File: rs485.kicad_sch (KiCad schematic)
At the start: 48 parts, among them J2101 RS485 Socket, Q2001 2N7002, U2102 ISO7741DBQ, U2104 SP3485EN-L/TR, U2105 SP3485EN-L/TR

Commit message: Fix schematic ERC errors
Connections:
- net GND2 renamed GND_RS485

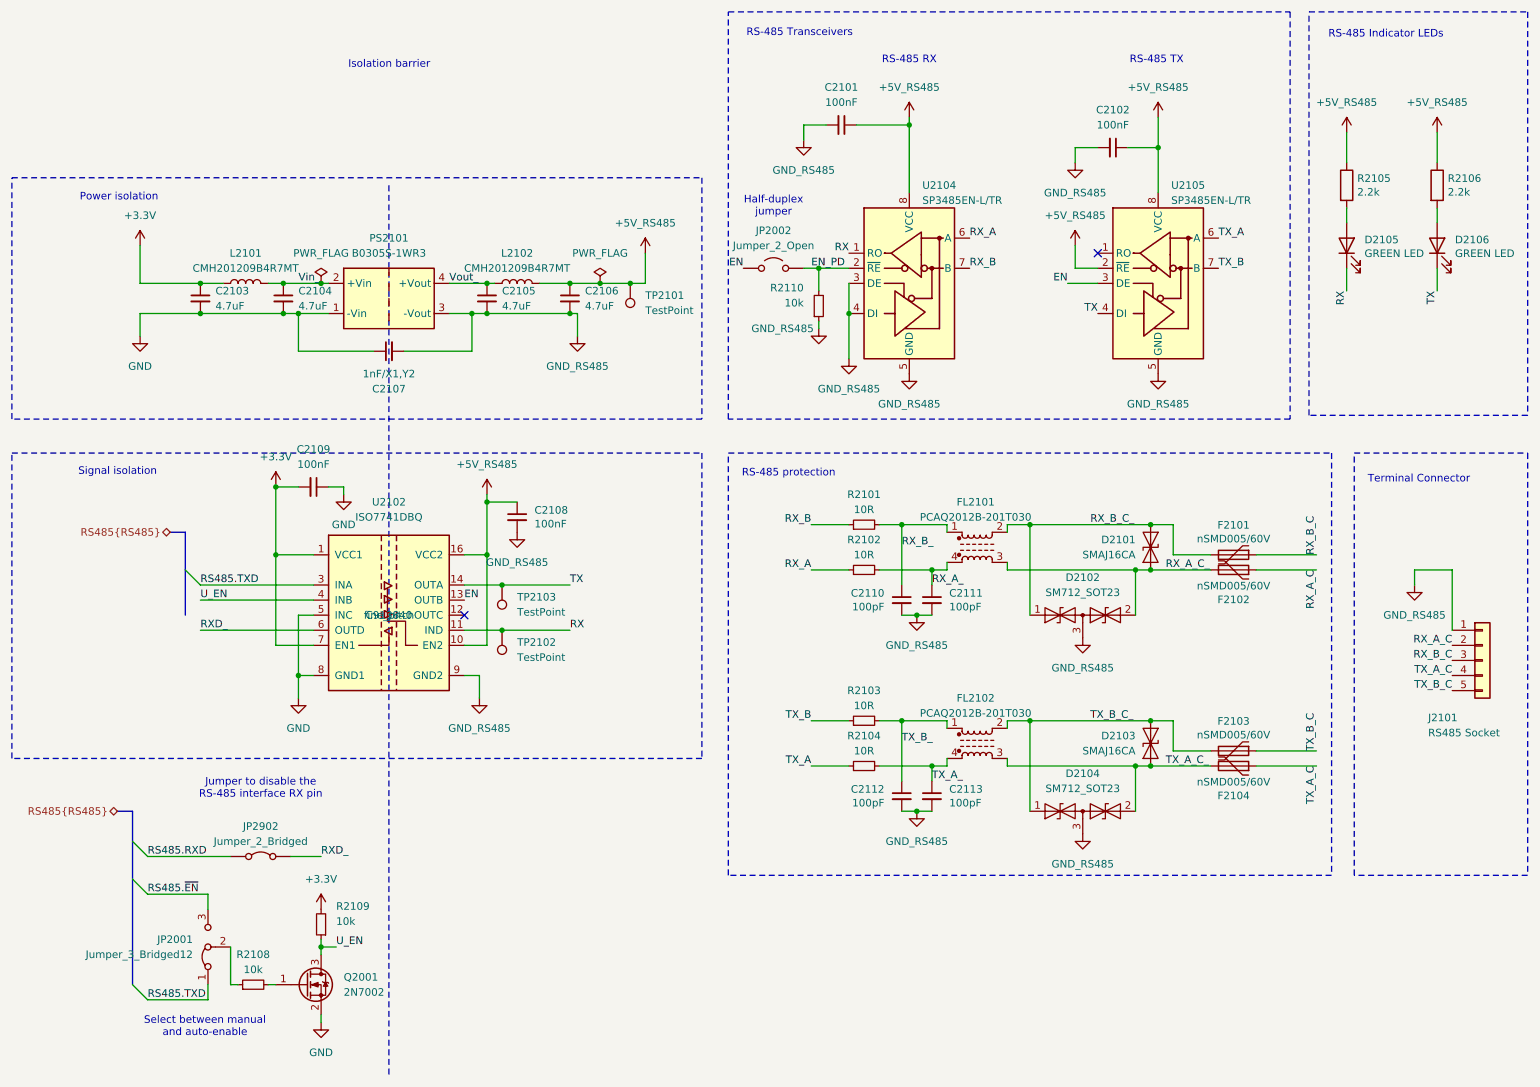
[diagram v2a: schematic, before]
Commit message: Reannotate components
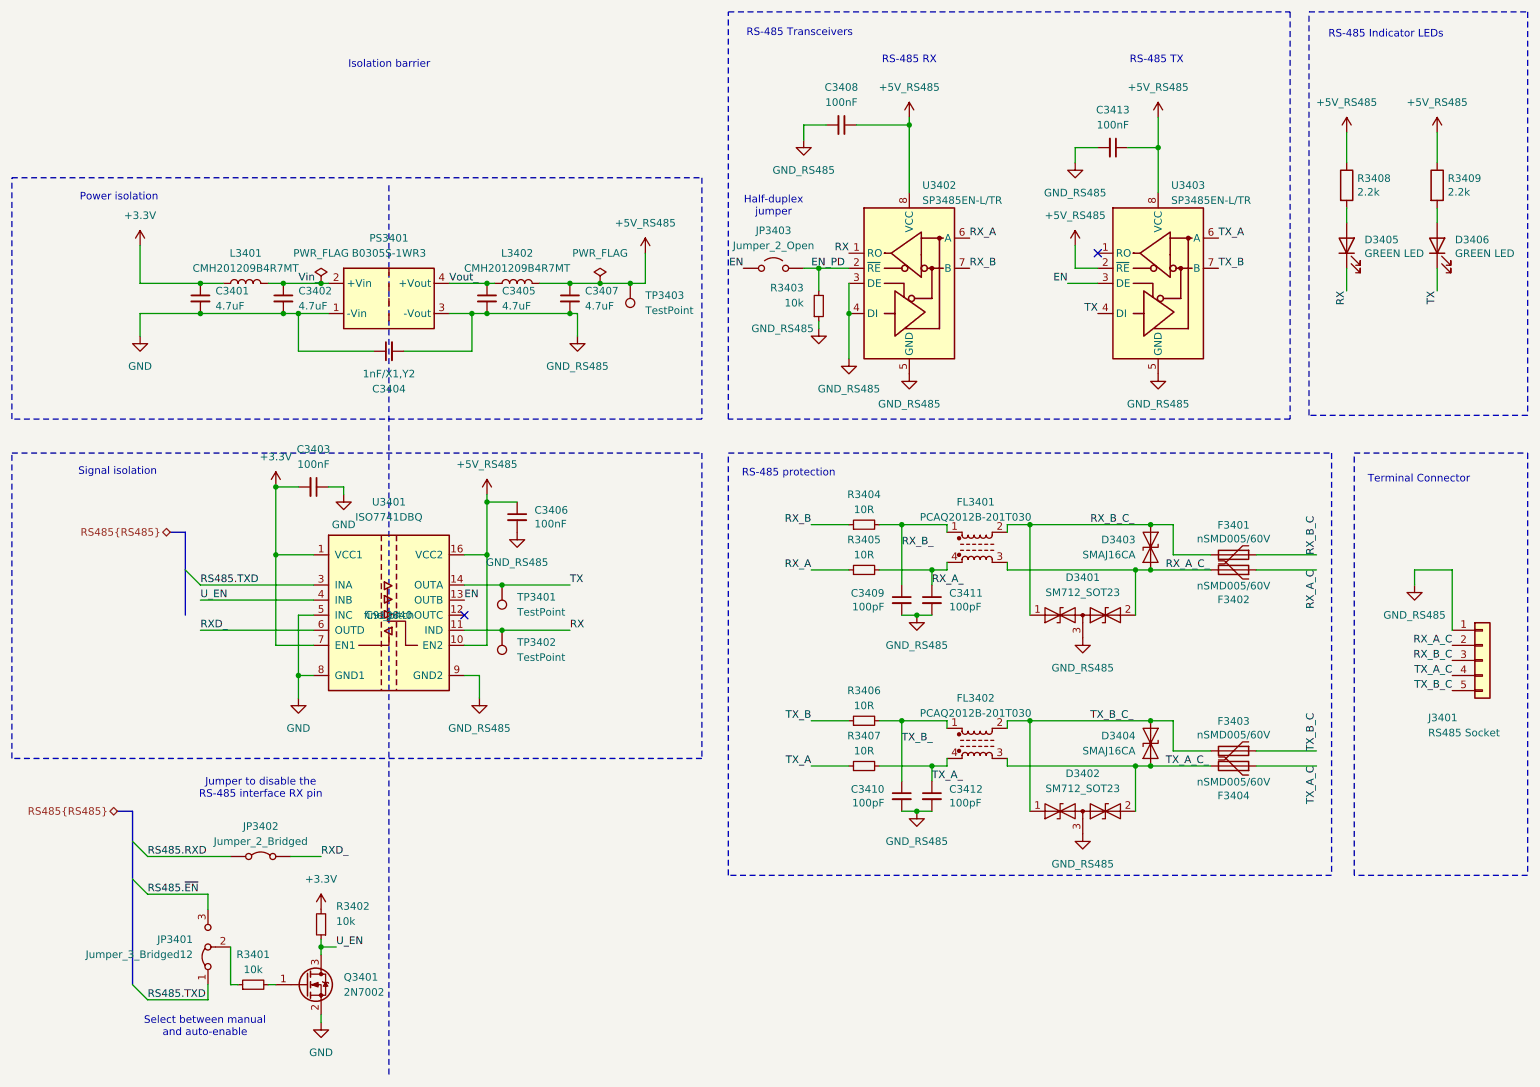
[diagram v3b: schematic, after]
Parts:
- renumbered C2103 to C3401, C2104 to C3402, C2109 to C3403, C2107 to C3404, C2105 to C3405, C2108 to C3406, C2106 to C3407, C2101 to C3408, C2110 to C3409, C2112 to C3410, C2111 to C3411, C2113 to C3412, C2102 to C3413, D2102 to D3401, D2104 to D3402, D2101 to D3403, D2103 to D3404, D2105 to D3405, D2106 to D3406, F2101 to F3401, F2102 to F3402, F2103 to F3403, F2104 to F3404, FL2101 to FL3401, FL2102 to FL3402, J2101 to J3401, JP2001 to JP3401, JP2902 to JP3402, JP2002 to JP3403, L2101 to L3401, L2102 to L3402, PS2101 to PS3401, Q2001 to Q3401, R2108 to R3401, R2109 to R3402, R2110 to R3403, R2101 to R3404, R2102 to R3405, R2103 to R3406, R2104 to R3407, R2105 to R3408, R2106 to R3409, TP2103 to TP3401, TP2102 to TP3402, TP2101 to TP3403, U2102 to U3401, U2104 to U3402, U2105 to U3403

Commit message: Most DRC errors fixed
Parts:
- JP3401: LCSC (none) -> C2937625
- JP3403: LCSC (none) -> C492401
- Q3401: LCSC (none) -> 2N7002
- R3401, R3402, R3403: LCSC (none) -> C25744
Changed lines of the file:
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@@
 		(polyline
 			(pts
-				(xy 54.61 110.49) (xy 54.61 121.92) (xy 52.07 121.92) (xy 52.07 110.49)
+				(xy 109.22 111.76) (xy 109.22 123.19) (xy 106.68 123.19) (xy 106.68 111.76)
 			)
 			(stroke
@@
 		(polyline
 			(pts
-				(xy 109.22 111.76) (xy 109.22 123.19) (xy 106.68 123.19) (xy 106.68 111.76)
+				(xy 54.61 110.49) (xy 54.61 121.92) (xy 52.07 121.92) (xy 52.07 110.49)
 			)
 			(stroke
@@
 			)
 		)
-		(property "LCSC" ""
+		(property "LCSC" "C25744"
 			(at 57.15 180.34 0)
 			(effects
@@
 			)
 		)
+		(property "LCSC" "C2937625"
+			(at 49.53 173.99 0)
+			(effects
+				(font
+					(size 1.27 1.27)
+				)
+			)
+		)
 		(pin "3"
 		)
@@
 			)
 		)
-		(property "LCSC" ""
+		(property "LCSC" "C25744"
 			(at 152.4 66.04 0)
 			(effects
@@
 			)
 		)
-		(property "LCSC" ""
+		(property "LCSC" "C25744"
 			(at 68.58 170.18 0)
 			(effects
@@
 			)
 		)
+		(property "LCSC" "2N7002"
+			(at 66.04 180.34 0)
+			(effects
+				(font
+					(size 1.27 1.27)
+				)
+			)
+		)
 		(pin "3"
 		)
@@
 			)
 		)
+		(property "LCSC" "C492401"
+			(at 144.78 59.69 0)
+			(effects
+				(font
+					(size 1.27 1.27)
+				)
+			)
+		)
 		(pin "2"
 		)
@@
 					(size 1.27 1.27)
 				)
+				(hide yes)
 			)
 		)
@@
 					(size 1.27 1.27)
 				)
+				(hide yes)
 			)
 		)

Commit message: Silkscreen mostly done
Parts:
- C3403, C3406, C3408, C3413: value 100nF -> 1uF; LCSC C1525 -> C52923
- D3402: Component Class (none) -> fine_pitch
- Q3401: LCSC 2N7002 -> C8545
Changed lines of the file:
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@@
 			)
 		)
-		(property "Value" "100nF"
+		(property "Value" "1uF"
 			(at 156.2036 31.75 90)
 			(effects
@@
 			)
 		)
-		(property "LCSC" "C1525"
+		(property "LCSC" "C52923"
 			(at 156.21 35.56 0)
 			(effects
@@
 			)
 		)
+		(property "Component Class" "fine_pitch"
+			(at 196.85 151.13 0)
+			(effects
+				(font
+					(size 1.27 1.27)
+				)
+			)
+		)
 		(pin "3"
 		)
@@
 					(size 1.27 1.27)
 				)
+				(hide yes)
 			)
 		)
@@
 			)
 		)
-		(property "Value" "100nF"
+		(property "Value" "1uF"
 			(at 67.3036 92.71 90)
 			(effects
@@
 			)
 		)
-		(property "LCSC" "C1525"
+		(property "LCSC" "C52923"
 			(at 67.31 96.52 0)
 			(effects
@@
 			)
 		)
-		(property "LCSC" "2N7002"
+		(property "LCSC" "C8545"
 			(at 66.04 180.34 0)
 			(effects
@@
 					(size 1.27 1.27)
 				)
+				(hide yes)
 			)
 		)
@@
 					(size 1.27 1.27)
 				)
+				(hide yes)
 			)
 		)
@@
 			)
 		)
-		(property "Value" "100nF"
+		(property "Value" "1uF"
 			(at 104.521 102.743 0)
 			(effects
@@
 			)
 		)
-		(property "LCSC" "C1525"
+		(property "LCSC" "C52923"
 			(at 101.6 101.6 0)
 			(effects
@@
 			)
 		)
-		(property "Value" "100nF"
+		(property "Value" "1uF"
 			(at 201.9236 35.56 90)
 			(effects
@@
 			)
 		)
-		(property "LCSC" "C1525"
+		(property "LCSC" "C52923"
 			(at 201.93 39.37 0)
 			(effects

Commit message: Finish the board redesign with SoM on the bottom
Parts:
- D3403, D3404: footprint PCM_Diode_SMD_AKL:D_SMA_TVS -> Diode_SMD:D_SMA
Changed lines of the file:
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@@
 			)
 		)
-		(property "Datasheet" "https://www.lcsc.com/datasheet/lcsc_datasheet_2304140030_MaxLinear-SP3485EN-L-TR_C8963.pdf"
+		(property "Datasheet" "http://www.icbase.com/pdf/SPX/SPX00480106.pdf"
 			(at 167.64 62.23 0)
 			(effects
@@
 			)
 		)
-		(property "Description" "Power symbol creates a global label with name \"CMx_3V3_CAN\""
+		(property "Description" "Power symbol creates a global label with name \"+3V3_CAN\""
 			(at 96.52 97.79 0)
 			(effects
@@
 			)
 		)
-		(property "Description" ""
+		(property "Description" "Resettable fuse, polymeric positive temperature coefficient"
 			(at 222.25 143.51 0)
 			(effects
@@
 			)
 		)
-		(property "Description" ""
+		(property "Description" "Resistor"
 			(at 241.3 45.72 0)
 			(effects
@@
 			)
 		)
-		(property "Description" ""
+		(property "Description" "Resettable fuse, polymeric positive temperature coefficient"
 			(at 222.25 107.95 0)
 			(effects
@@
 			)
 		)
-		(property "Description" ""
+		(property "Description" "Inductor"
 			(at 55.88 62.23 0)
 			(effects
@@
 			)
 		)
-		(property "Description" ""
+		(property "Description" "Resettable fuse, polymeric positive temperature coefficient"
 			(at 222.25 110.49 0)
 			(effects
@@
 			)
 		)
-		(property "Description" ""
+		(property "Description" "Light emitting diode"
 			(at 241.3 55.88 0)
 			(effects
@@
 			)
 		)
-		(property "Sim.Pins" ""
+		(property "Sim.Pins" "1=K 2=A"
 			(at 241.3 55.88 0)
 			(effects
@@
 			)
 		)
-		(property "Footprint" "PCM_Diode_SMD_AKL:D_SMA_TVS"
+		(property "Footprint" "Diode_SMD:D_SMA"
 			(at 203.2 139.7 0)
 			(effects
@@
 			)
 		)
-		(property "Footprint" "PCM_Diode_SMD_AKL:D_SMA_TVS"
+		(property "Footprint" "Diode_SMD:D_SMA"
 			(at 203.2 106.68 0)
 			(effects
@@
 			)
 		)
-		(property "Description" ""
+		(property "Description" "Unpolarized capacitor, small symbol"
 			(at 96.52 64.77 0)
 			(effects
@@
 			)
 		)
-		(property "Description" ""
+		(property "Description" "Unpolarized capacitor, small symbol"
 			(at 110.49 64.77 0)
 			(effects
@@
 			)
 		)
-		(property "Description" ""
+		(property "Description" "Resistor"
 			(at 256.54 45.72 0)
 			(effects
@@
 			)
 		)
-		(property "Datasheet" "https://www.lcsc.com/datasheet/lcsc_datasheet_2304140030_MaxLinear-SP3485EN-L-TR_C8963.pdf"
+		(property "Datasheet" "http://www.icbase.com/pdf/SPX/SPX00480106.pdf"
 			(at 209.55 62.23 0)
 			(effects
@@
 			)
 		)
-		(property "Description" ""
+		(property "Description" "Unpolarized capacitor, small symbol"
 			(at 62.23 64.77 0)
 			(effects
@@
 			)
 		)
-		(property "Description" ""
+		(property "Description" "Unpolarized capacitor, small symbol"
 			(at 67.31 96.52 0)
 			(effects
@@
 			)
 		)
-		(property "Description" ""
+		(property "Description" "Resettable fuse, polymeric positive temperature coefficient"
 			(at 222.25 140.97 0)
 			(effects
@@
 			)
 		)
-		(property "Description" ""
+		(property "Description" "Inductor"
 			(at 101.6 62.23 0)
 			(effects
@@
 			)
 		)
-		(property "Description" ""
+		(property "Description" "Light emitting diode"
 			(at 256.54 55.88 0)
 			(effects
@@
 			)
 		)
-		(property "Sim.Pins" ""
+		(property "Sim.Pins" "1=K 2=A"
 			(at 256.54 55.88 0)
 			(effects
@@
 			)
 		)
-		(property "Description" ""
+		(property "Description" "Unpolarized capacitor, small symbol"
 			(at 101.6 101.6 0)
 			(effects
@@
 			)
 		)
-		(property "Description" ""
+		(property "Description" "Unpolarized capacitor, small symbol"
 			(at 48.26 64.77 0)
 			(effects
@@
 			)
 		)
-		(property "Description" ""
+		(property "Description" "Unpolarized capacitor, small symbol"
 			(at 80.01 73.66 0)
 			(effects

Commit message: Further refinements
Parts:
- U3401: value ISO7741DBQ -> π141M31; footprint Package_SO:SSOP-16_3.9x4.9mm_P0.635mm -> Package_SO:SOIC-16_3.9x9.9mm_P1.27mm; LCSC C913840 -> C471605; Notes (none) -> Alt. ISO7741
